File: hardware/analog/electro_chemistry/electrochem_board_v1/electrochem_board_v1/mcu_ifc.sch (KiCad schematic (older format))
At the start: 1 part

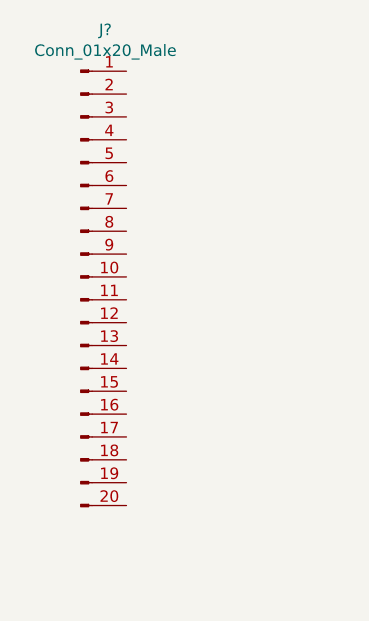
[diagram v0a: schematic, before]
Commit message: Electrochemistry board: preparing the layout
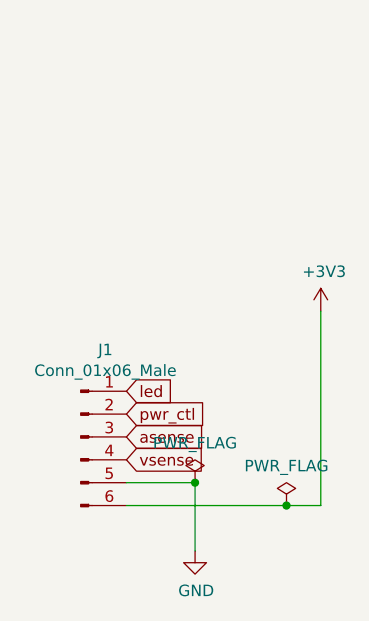
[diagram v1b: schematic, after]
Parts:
- removed J?: Conn_01x20_Male, symbol Connector:Conn_01x20_Male
- added J1: Conn_01x06_Male, Connector_PinSocket_2.54mm:PinSocket_1x06_P2.54mm_Vertical, symbol Connector:Conn_01x06_Male
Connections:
- new net +3V3: J1.6 (Pin_6)
- new net GND: J1.5 (Pin_5)
- new net asense: J1.3 (Pin_3)
- new net led: J1.1 (Pin_1)
- new net pwr_ctl: J1.2 (Pin_2)
- new net vsense: J1.4 (Pin_4)
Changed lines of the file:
@@
 $EndDescr
 $Comp
-L Connector:Conn_01x20_Male J?
-U 1 1 6096EB1E
-P 3500 3800
-F 0 "J?" H 3608 4881 50  0000 C CNN
-F 1 "Conn_01x20_Male" H 3608 4790 50  0000 C CNN
-F 2 "" H 3500 3800 50  0001 C CNN
-F 3 "~" H 3500 3800 50  0001 C CNN
-	1    3500 3800
+L power:GND #PWR01
+U 1 1 60A0449C
+P 4000 5000
+F 0 "#PWR01" H 4000 4750 50  0001 C CNN
+F 1 "GND" H 4005 4827 50  0000 C CNN
+F 2 "" H 4000 5000 50  0001 C CNN
+F 3 "" H 4000 5000 50  0001 C CNN
+	1    4000 5000
 	1    0    0    -1
 $EndComp
+Wire Wire Line
+	3700 4700 4000 4700
+Wire Wire Line
+	4000 4700 4000 5000
+Text GLabel 3700 4600 2    50   Input ~ 0
+vsense
+Text GLabel 3700 4500 2    50   Input ~ 0
+asense
+Text GLabel 3700 4400 2    50   Input ~ 0
+pwr_ctl
+$Comp
+L Connector:Conn_01x06_Male J1
+U 1 1 60A0AD14
+P 3500 4500
+F 0 "J1" H 3608 4881 50  0000 C CNN
+F 1 "Conn_01x06_Male" H 3608 4790 50  0000 C CNN
+F 2 "Connector_PinSocket_2.54mm:PinSocket_1x06_P2.54mm_Vertical" H 3500 4500 50  0001 C CNN
+F 3 "~" H 3500 4500 50  0001 C CNN
+	1    3500 4500
+	1    0    0    -1
+$EndComp
+$Comp
+L power:+3V3 #PWR02
+U 1 1 60A0B9A9
+P 4550 3950
+F 0 "#PWR02" H 4550 3800 50  0001 C CNN
+F 1 "+3V3" H 4565 4123 50  0000 C CNN
+F 2 "" H 4550 3950 50  0001 C CNN
+F 3 "" H 4550 3950 50  0001 C CNN
+	1    4550 3950
+	1    0    0    -1
+$EndComp
+Wire Wire Line
+	3700 4800 4400 4800
+Wire Wire Line
+	4550 4800 4550 3950
+$Comp
+L power:PWR_FLAG #FLG02
+U 1 1 60A0BFC0
+P 4400 4800
+F 0 "#FLG02" H 4400 4875 50  0001 C CNN
+F 1 "PWR_FLAG" H 4400 4973 50  0000 C CNN
+F 2 "" H 4400 4800 50  0001 C CNN
+F 3 "~" H 4400 4800 50  0001 C CNN
+	1    4400 4800
+	1    0    0    -1
+$EndComp
+Connection ~ 4400 4800
+Wire Wire Line
+	4400 4800 4550 4800
+$Comp
+L power:PWR_FLAG #FLG01
+U 1 1 60A0C34D
+P 4000 4700
+F 0 "#FLG01" H 4000 4775 50  0001 C CNN
+F 1 "PWR_FLAG" H 4000 4873 50  0000 C CNN
+F 2 "" H 4000 4700 50  0001 C CNN
+F 3 "~" H 4000 4700 50  0001 C CNN
+	1    4000 4700
+	1    0    0    -1
+$EndComp
+Connection ~ 4000 4700
+Text GLabel 3700 4300 2    50   Input ~ 0
+led
 $EndSCHEMATC
